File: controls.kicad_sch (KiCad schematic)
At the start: 0 parts

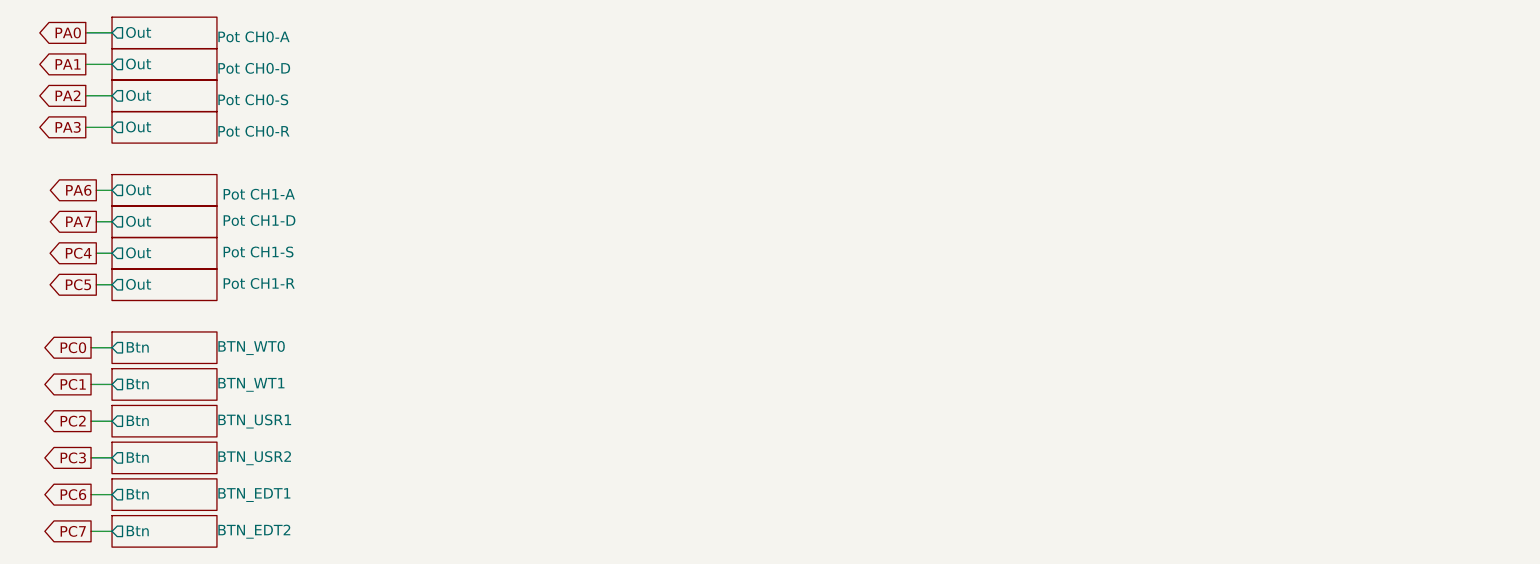
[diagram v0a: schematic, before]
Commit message: reannotated changed to LM324
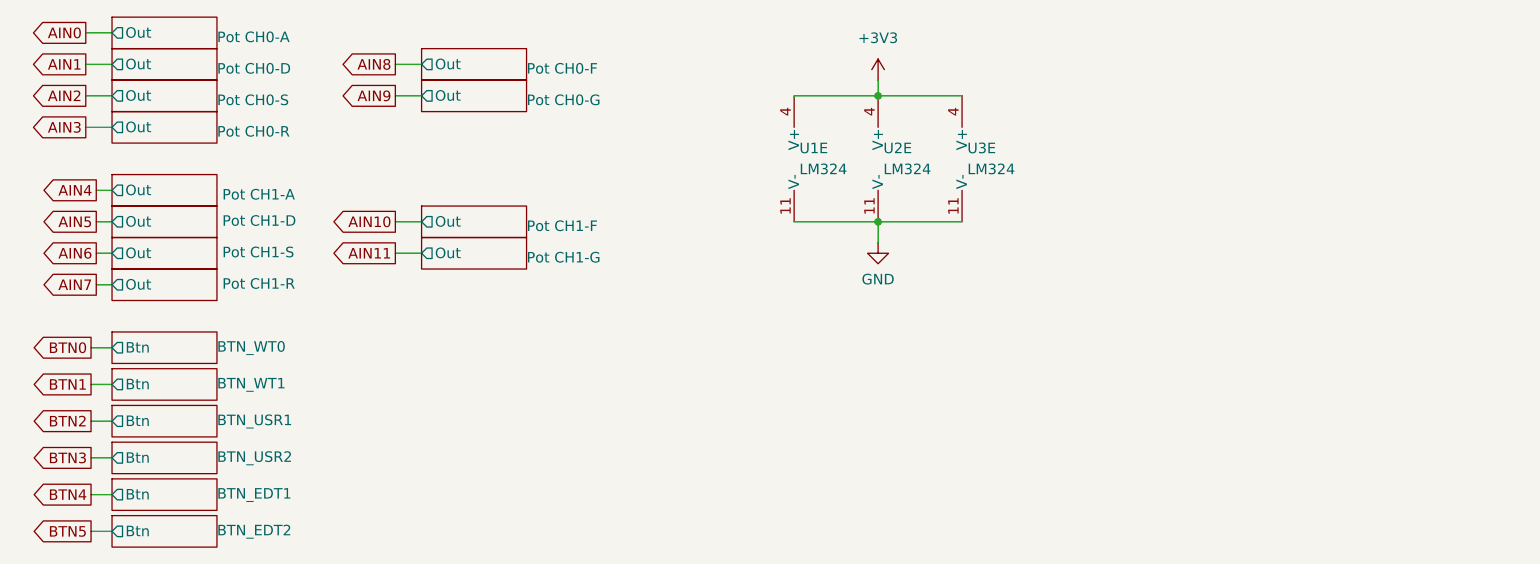
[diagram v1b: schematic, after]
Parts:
- added U1, U2, U3: LM324, Package_SO:SO-14_3.9x8.65mm_P1.27mm, symbol eurorack:LM324
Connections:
- new net +3V3: U1.4 (V+), U2.4 (V+), U3.4 (V+)
- new net GND: U1.11 (V-), U2.11 (V-), U3.11 (V-)
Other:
- added sheet Pot CH0-F (pot.kicad_sch)
- added sheet Pot CH0-G (pot.kicad_sch)
- added sheet Pot CH1-F (pot.kicad_sch)
- added sheet Pot CH1-G (pot.kicad_sch)

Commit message: reworking with Pot Lights
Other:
- sheet Pot CH0-A ports: added LED; removed none
- sheet Pot CH0-D ports: added LED; removed none
- sheet Pot CH0-F ports: added LED; removed none
- sheet Pot CH0-G ports: added LED; removed none
- sheet Pot CH0-R ports: added LED; removed none
- sheet Pot CH0-S ports: added LED; removed none
- sheet Pot CH1-A ports: added LED; removed none
- sheet Pot CH1-D ports: added LED; removed none
- sheet Pot CH1-F ports: added LED; removed none
- sheet Pot CH1-G ports: added LED; removed none
- sheet Pot CH1-R ports: added LED; removed none
- sheet Pot CH1-S ports: added LED; removed none
- moved on the sheet: U1E, U2E, U3E

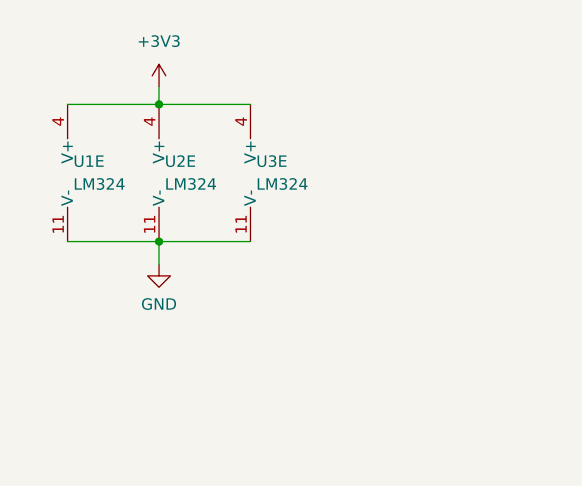
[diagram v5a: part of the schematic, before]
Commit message: working on lifted leds
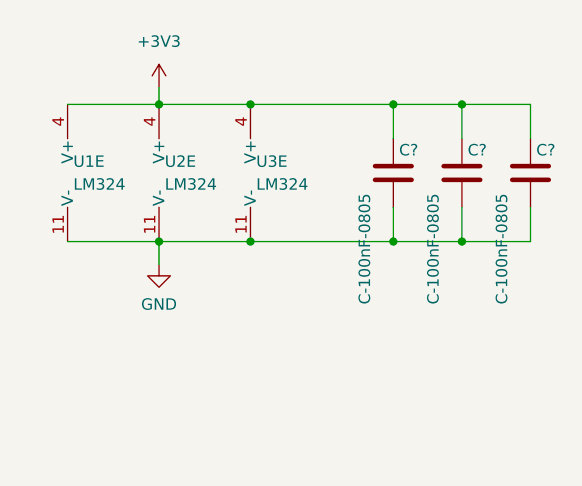
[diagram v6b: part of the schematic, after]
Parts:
- added C? (x3): C-100nF-0805, Capacitor_SMD:C_0805_2012Metric_Pad1.18x1.45mm_HandSolder, symbol eurorack:C-100nF-0805
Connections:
- net +3V3: now also C?.1, C?.1, C?.1
- net GND: now also C?.2, C?.2, C?.2
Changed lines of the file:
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@@
 (kicad_sch (version 20211123) (generator eeschema)
   (paper "A4")
+  (junction (at 196.85 46.355) (diameter 0) (color 0 0 0 0)
+  )
+  (junction (at 196.85 31.115) (diameter 0) (color 0 0 0 0)
+  )
+  (junction (at 173.355 31.115) (diameter 0) (color 0 0 0 0)
+  )
+  (junction (at 189.23 31.115) (diameter 0) (color 0 0 0 0)
+  )
+  (junction (at 189.23 46.355) (diameter 0) (color 0 0 0 0)
+  )
+  (junction (at 173.355 46.355) (diameter 0) (color 0 0 0 0)
+  )
   (junction (at 163.195 31.115) (diameter 0) (color 0 0 0 0)
   )
@@
     (stroke (width 0) (type default) (color 0 0 0 0))
   )
+  (wire (pts (xy 189.23 46.355) (xy 173.355 46.355))
+    (stroke (width 0) (type default) (color 0 0 0 0))
+  )
   (wire (pts (xy 85.725 31.115) (xy 88.9 31.115))
     (stroke (width 0) (type default) (color 0 0 0 0))
   )
+  (wire (pts (xy 196.85 46.355) (xy 189.23 46.355))
+    (stroke (width 0) (type default) (color 0 0 0 0))
+  )
   (wire (pts (xy 163.195 29.21) (xy 163.195 31.115))
     (stroke (width 0) (type default) (color 0 0 0 0))
@@
     (stroke (width 0) (type default) (color 0 0 0 0))
   )
+  (wire (pts (xy 204.47 46.355) (xy 196.85 46.355))
+    (stroke (width 0) (type default) (color 0 0 0 0))
+  )
   (wire (pts (xy 36.195 66.04) (xy 38.735 66.04))
     (stroke (width 0) (type default) (color 0 0 0 0))
   )
+  (wire (pts (xy 204.47 31.115) (xy 204.47 34.925))
+    (stroke (width 0) (type default) (color 0 0 0 0))
+  )
   (wire (pts (xy 36.83 53.975) (xy 38.735 53.975))
     (stroke (width 0) (type default) (color 0 0 0 0))
@@
     (stroke (width 0) (type default) (color 0 0 0 0))
   )
+  (wire (pts (xy 173.355 31.115) (xy 189.23 31.115))
+    (stroke (width 0) (type default) (color 0 0 0 0))
+  )
+  (wire (pts (xy 189.23 31.115) (xy 189.23 34.925))
+    (stroke (width 0) (type default) (color 0 0 0 0))
+  )
   (wire (pts (xy 51.435 53.975) (xy 52.705 53.975))
     (stroke (width 0) (type default) (color 0 0 0 0))
   )
+  (wire (pts (xy 189.23 42.545) (xy 189.23 46.355))
+    (stroke (width 0) (type default) (color 0 0 0 0))
+  )
   (wire (pts (xy 35.56 31.115) (xy 38.735 31.115))
     (stroke (width 0) (type default) (color 0 0 0 0))
@@
     (stroke (width 0) (type default) (color 0 0 0 0))
   )
+  (wire (pts (xy 196.85 31.115) (xy 196.85 34.925))
+    (stroke (width 0) (type default) (color 0 0 0 0))
+  )
   (wire (pts (xy 51.435 42.545) (xy 52.705 42.545))
     (stroke (width 0) (type default) (color 0 0 0 0))
   )
+  (wire (pts (xy 189.23 31.115) (xy 196.85 31.115))
+    (stroke (width 0) (type default) (color 0 0 0 0))
+  )
   (wire (pts (xy 36.83 42.545) (xy 38.735 42.545))
     (stroke (width 0) (type default) (color 0 0 0 0))
@@
     (stroke (width 0) (type default) (color 0 0 0 0))
   )
+  (wire (pts (xy 196.85 42.545) (xy 196.85 46.355))
+    (stroke (width 0) (type default) (color 0 0 0 0))
+  )
+  (wire (pts (xy 196.85 31.115) (xy 204.47 31.115))
+    (stroke (width 0) (type default) (color 0 0 0 0))
+  )
   (wire (pts (xy 163.195 46.355) (xy 173.355 46.355))
     (stroke (width 0) (type default) (color 0 0 0 0))
@@
   )
   (wire (pts (xy 36.195 74.93) (xy 38.735 74.93))
+    (stroke (width 0) (type default) (color 0 0 0 0))
+  )
+  (wire (pts (xy 204.47 42.545) (xy 204.47 46.355))
     (stroke (width 0) (type default) (color 0 0 0 0))
   )
@@
     )
     (pin "1")
+  )
+  (symbol (lib_id "eurorack:C-100nF-0805") (at 196.85 38.735 0) (unit 1)
+    (in_bom yes) (on_board yes)
+    (property "Reference" "C?" (id 0) (at 197.485 36.195 0)
+      (effects (font (size 1.27 1.27)) (justify left))
+    )
+    (property "Value" "C-100nF-0805" (id 1) (at 193.675 53.34 90)
+      (effects (font (size 1.27 1.27)) (justify left))
+    )
+    (property "Footprint" "Capacitor_SMD:C_0805_2012Metric_Pad1.18x1.45mm_HandSolder" (id 2) (at 197.8152 42.545 0)
+      (effects (font (size 1.27 1.27)) hide)
+    )
+    (property "Datasheet" "https://secure.reichelt.com/at/en/smd-multilayer-ceramic-capacitor-100-n-10--x7r-g0805-100n-p31879.html?&nbc=1" (id 3) (at 196.85 38.735 0)
+      (effects (font (size 1.27 1.27)) hide)
+    )
+    (pin "1")
+    (pin "2")
+  )
+  (symbol (lib_id "eurorack:C-100nF-0805") (at 204.47 38.735 0) (unit 1)
+    (in_bom yes) (on_board yes)
+    (property "Reference" "C?" (id 0) (at 205.105 36.195 0)
+      (effects (font (size 1.27 1.27)) (justify left))
+    )
+    (property "Value" "C-100nF-0805" (id 1) (at 201.295 53.34 90)
+      (effects (font (size 1.27 1.27)) (justify left))
+    )
+    (property "Footprint" "Capacitor_SMD:C_0805_2012Metric_Pad1.18x1.45mm_HandSolder" (id 2) (at 205.4352 42.545 0)
+      (effects (font (size 1.27 1.27)) hide)
+    )
+    (property "Datasheet" "https://secure.reichelt.com/at/en/smd-multilayer-ceramic-capacitor-100-n-10--x7r-g0805-100n-p31879.html?&nbc=1" (id 3) (at 204.47 38.735 0)
+      (effects (font (size 1.27 1.27)) hide)
+    )
+    (pin "1")
+    (pin "2")
   )
   (symbol (lib_id "eurorack:LM324") (at 165.735 38.735 0) (unit 5)
@@
     (pin "4")
   )
+  (symbol (lib_id "eurorack:C-100nF-0805") (at 189.23 38.735 0) (unit 1)
+    (in_bom yes) (on_board yes)
+    (property "Reference" "C?" (id 0) (at 189.865 36.195 0)
+      (effects (font (size 1.27 1.27)) (justify left))
+    )
+    (property "Value" "C-100nF-0805" (id 1) (at 186.055 53.34 90)
+      (effects (font (size 1.27 1.27)) (justify left))
+    )
+    (property "Footprint" "Capacitor_SMD:C_0805_2012Metric_Pad1.18x1.45mm_HandSolder" (id 2) (at 190.1952 42.545 0)
+      (effects (font (size 1.27 1.27)) hide)
+    )
+    (property "Datasheet" "https://secure.reichelt.com/at/en/smd-multilayer-ceramic-capacitor-100-n-10--x7r-g0805-100n-p31879.html?&nbc=1" (id 3) (at 189.23 38.735 0)
+      (effects (font (size 1.27 1.27)) hide)
+    )
+    (pin "1")
+    (pin "2")
+  )
   (symbol (lib_id "eurorack:LM324") (at 155.575 38.735 0) (unit 5)

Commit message: wip led panel
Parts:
- gave numbers to parts that had none: 3
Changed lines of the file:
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@@
   (symbol (lib_id "eurorack:C-100nF-0805") (at 196.85 38.735 0) (unit 1)
     (in_bom yes) (on_board yes)
-    (property "Reference" "C?" (id 0) (at 197.485 36.195 0)
+    (property "Reference" "C38" (id 0) (at 197.485 36.195 0)
       (effects (font (size 1.27 1.27)) (justify left))
     )
@@
   (symbol (lib_id "eurorack:C-100nF-0805") (at 204.47 38.735 0) (unit 1)
     (in_bom yes) (on_board yes)
-    (property "Reference" "C?" (id 0) (at 205.105 36.195 0)
+    (property "Reference" "C39" (id 0) (at 205.105 36.195 0)
       (effects (font (size 1.27 1.27)) (justify left))
     )
@@
   (symbol (lib_id "eurorack:C-100nF-0805") (at 189.23 38.735 0) (unit 1)
     (in_bom yes) (on_board yes)
-    (property "Reference" "C?" (id 0) (at 189.865 36.195 0)
+    (property "Reference" "C37" (id 0) (at 189.865 36.195 0)
       (effects (font (size 1.27 1.27)) (justify left))
     )

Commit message: yet an other new version with 3 boards
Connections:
- net GND renamed GND3
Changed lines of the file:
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@@
     )
-  )
-  (symbol (lib_id "power:GND") (at 163.195 48.895 0) (unit 1)
-    (in_bom yes) (on_board yes) (fields_autoplaced)
-    (property "Reference" "#PWR095" (id 0) (at 163.195 55.245 0)
-      (effects (font (size 1.27 1.27)) hide)
-    )
-    (property "Value" "GND" (id 1) (at 163.195 53.34 0))
-    (property "Footprint" "" (id 2) (at 163.195 48.895 0)
-      (effects (font (size 1.27 1.27)) hide)
-    )
-    (property "Datasheet" "" (id 3) (at 163.195 48.895 0)
-      (effects (font (size 1.27 1.27)) hide)
-    )
-    (pin "1")
   )
   (symbol (lib_id "eurorack:C-100nF-0805") (at 196.85 38.735 0) (unit 1)
@@
     (pin "4")
   )
+  (symbol (lib_id "power:GND3") (at 163.195 48.895 0) (unit 1)
+    (in_bom yes) (on_board yes) (fields_autoplaced)
+    (property "Reference" "#PWR0151" (id 0) (at 163.195 55.245 0)
+      (effects (font (size 1.27 1.27)) hide)
+    )
+    (property "Value" "GND3" (id 1) (at 163.195 53.34 0))
+    (property "Footprint" "" (id 2) (at 163.195 48.895 0)
+      (effects (font (size 1.27 1.27)) hide)
+    )
+    (property "Datasheet" "" (id 3) (at 163.195 48.895 0)
+      (effects (font (size 1.27 1.27)) hide)
+    )
+    (pin "1")
+  )
   (symbol (lib_id "power:+3V3") (at 163.195 29.21 0) (unit 1)
